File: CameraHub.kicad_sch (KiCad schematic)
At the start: 19 parts, among them J1 200528-0100, J10 TE_282834-4, J2 Header 01x04 0.1", J3 Header 01x04 0.1", U14 TLV76733QWDRBxQ1

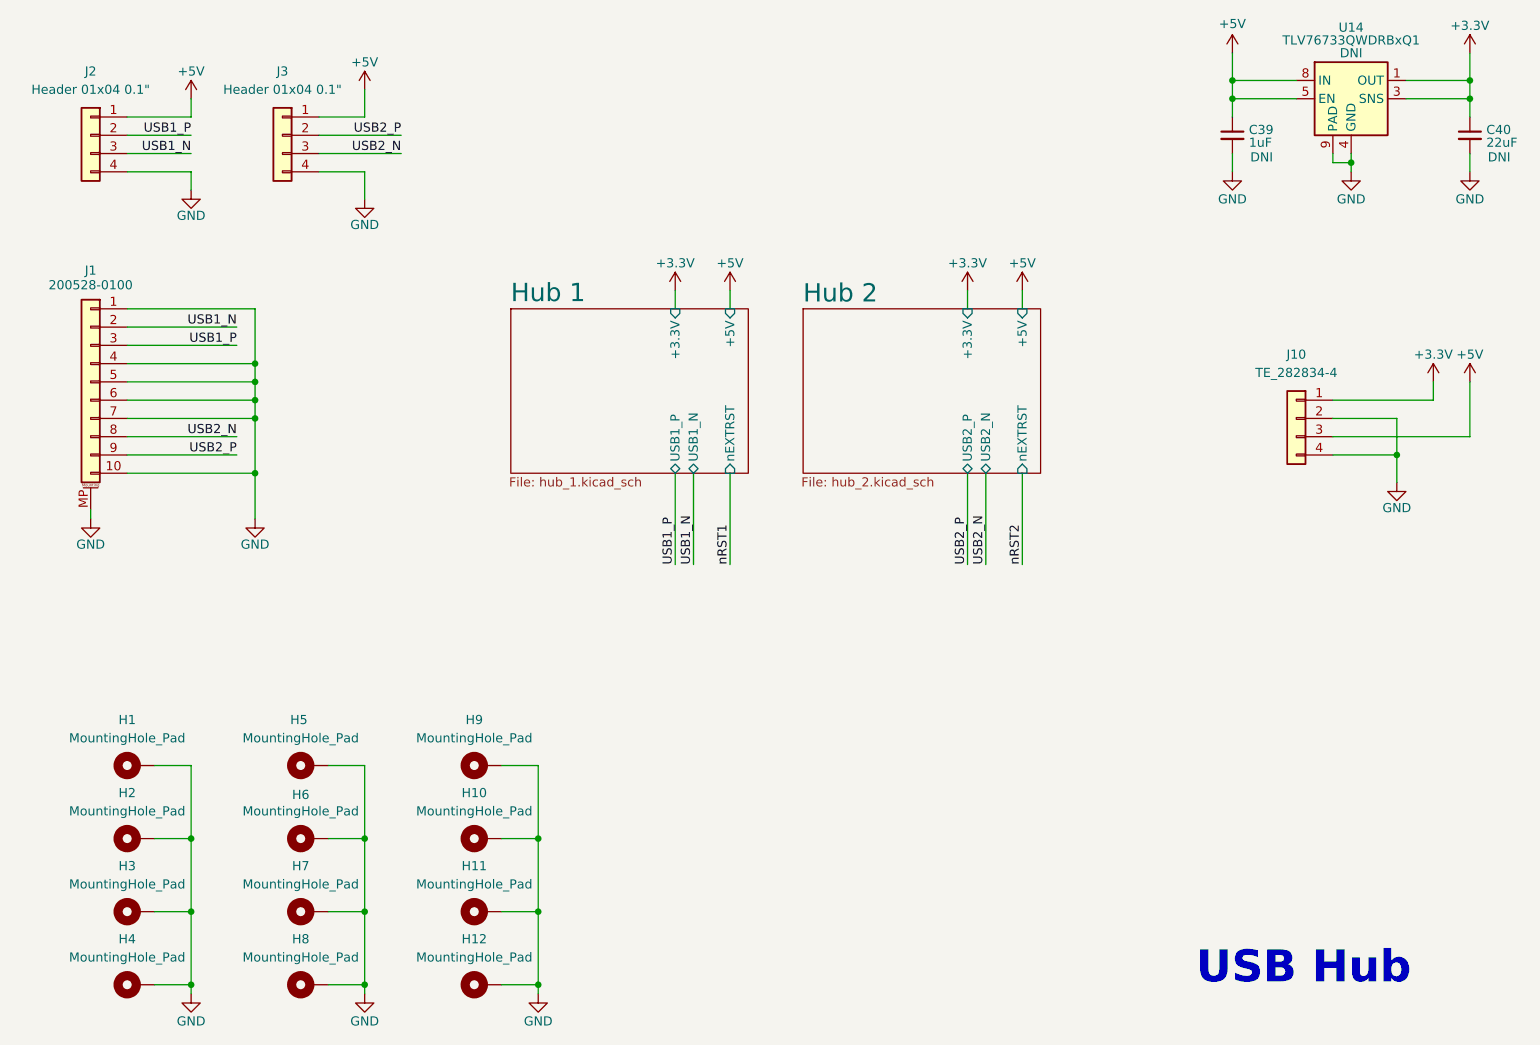
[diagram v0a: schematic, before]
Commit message: Updated for single USB line
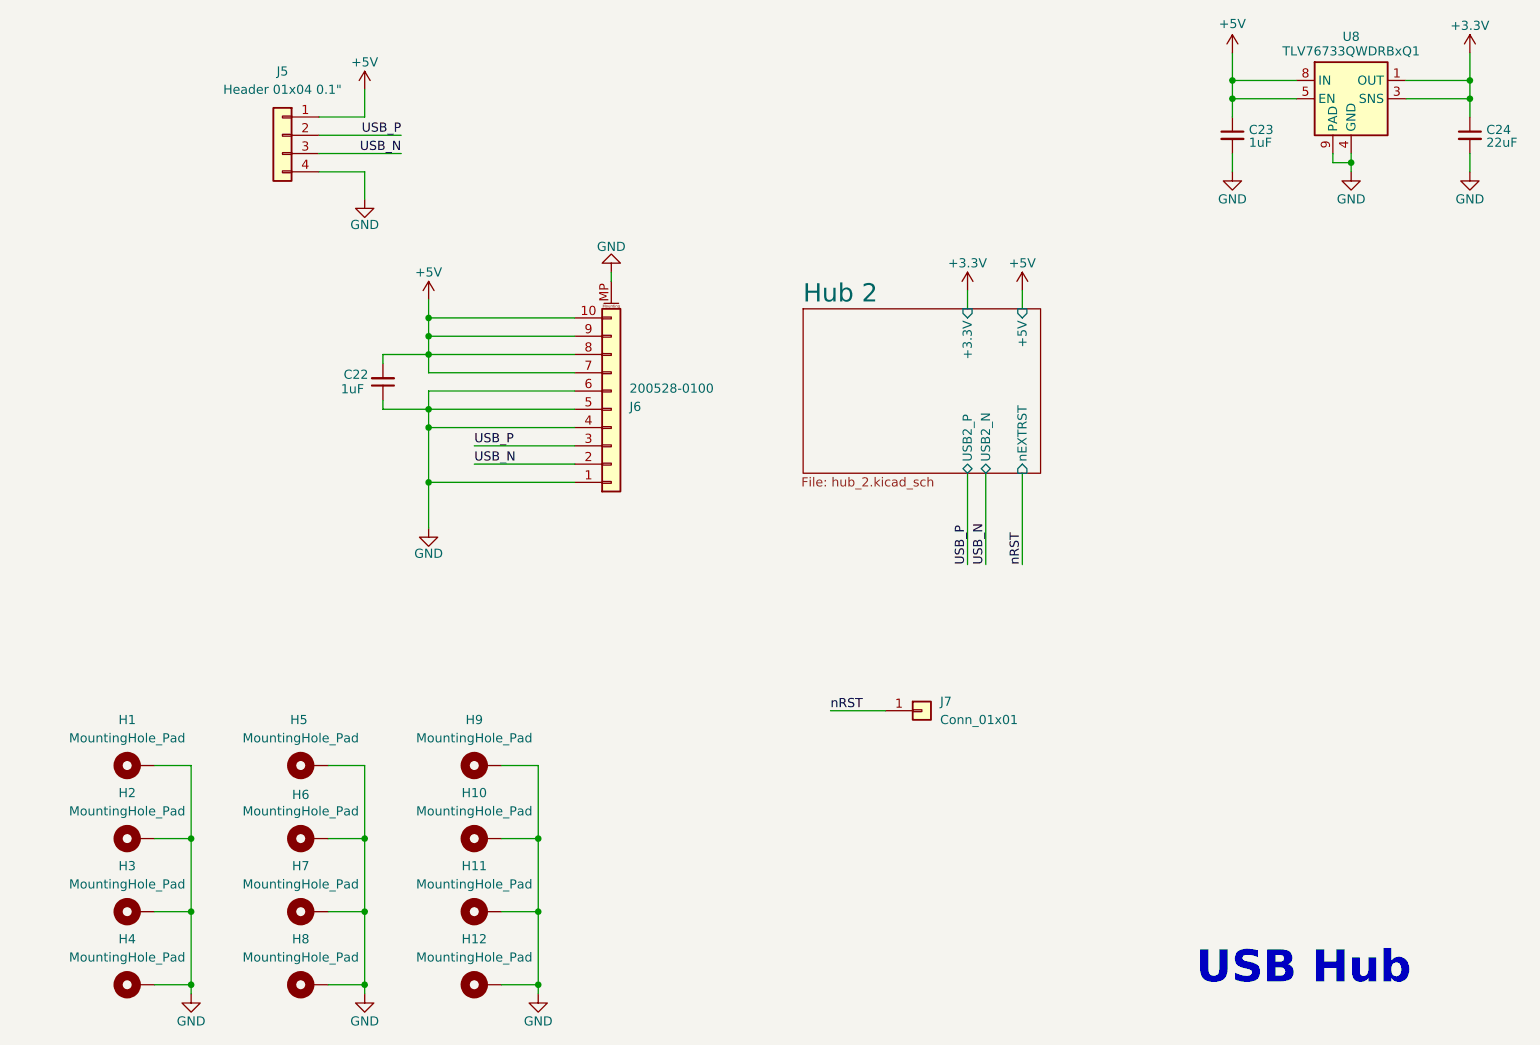
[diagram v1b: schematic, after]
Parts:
- removed J1: 200528-0100, Connector_FFC-FPC:Molex_200528-0100_1x10-1MP_P1.00mm_Horizontal, symbol Connector_Generic_MountingPin:Conn_01x10_MountingPin
- removed J10: TE_282834-4, CameraHub:TE_282834-4, symbol Connector_Generic:Conn_01x04
- removed J2: Header 01x04 0.1", Connector_PinHeader_2.54mm:PinHeader_1x04_P2.54mm_Vertical, symbol Connector_Generic:Conn_01x04
- added C22: 1uF, Capacitor_SMD:C_0603_1608Metric, symbol Device:C_Small
- added J6: 200528-0100, Connector_FFC-FPC:Molex_200528-0100_1x10-1MP_P1.00mm_Horizontal, symbol Connector_Generic_MountingPin:Conn_01x10_MountingPin
- added J7: Conn_01x01, TestPoint:TestPoint_Pad_D1.0mm, symbol Connector_Generic:Conn_01x01
- renumbered C39 to C23, C40 to C24, J3 to J5, U14 to U8
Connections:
- net +5V: now also C22.2, J6.10 (Pin_10), J6.7 (Pin_7), J6.8 (Pin_8), J6.9 (Pin_9)
- net GND: now also C22.1, J6.1 (Pin_1), J6.4 (Pin_4), J6.5 (Pin_5), J6.6 (Pin_6), J6.MP (MountPin)
- net USB2_N renamed USB_N
- net USB_N: now also J6.2 (Pin_2)
- net USB2_P renamed USB_P
- net USB_P: now also J6.3 (Pin_3)
- new net nRST: J7.1 (Pin_1)
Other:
- removed sheet Hub 1
